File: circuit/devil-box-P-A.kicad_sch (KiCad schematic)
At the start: 17 parts, among them M1 Motor_Servo, SW1 SW_Push, T1 BSS83P, T2 BSS83P, T3 BSS83P, T4 BUZ11, T5 BSS83P

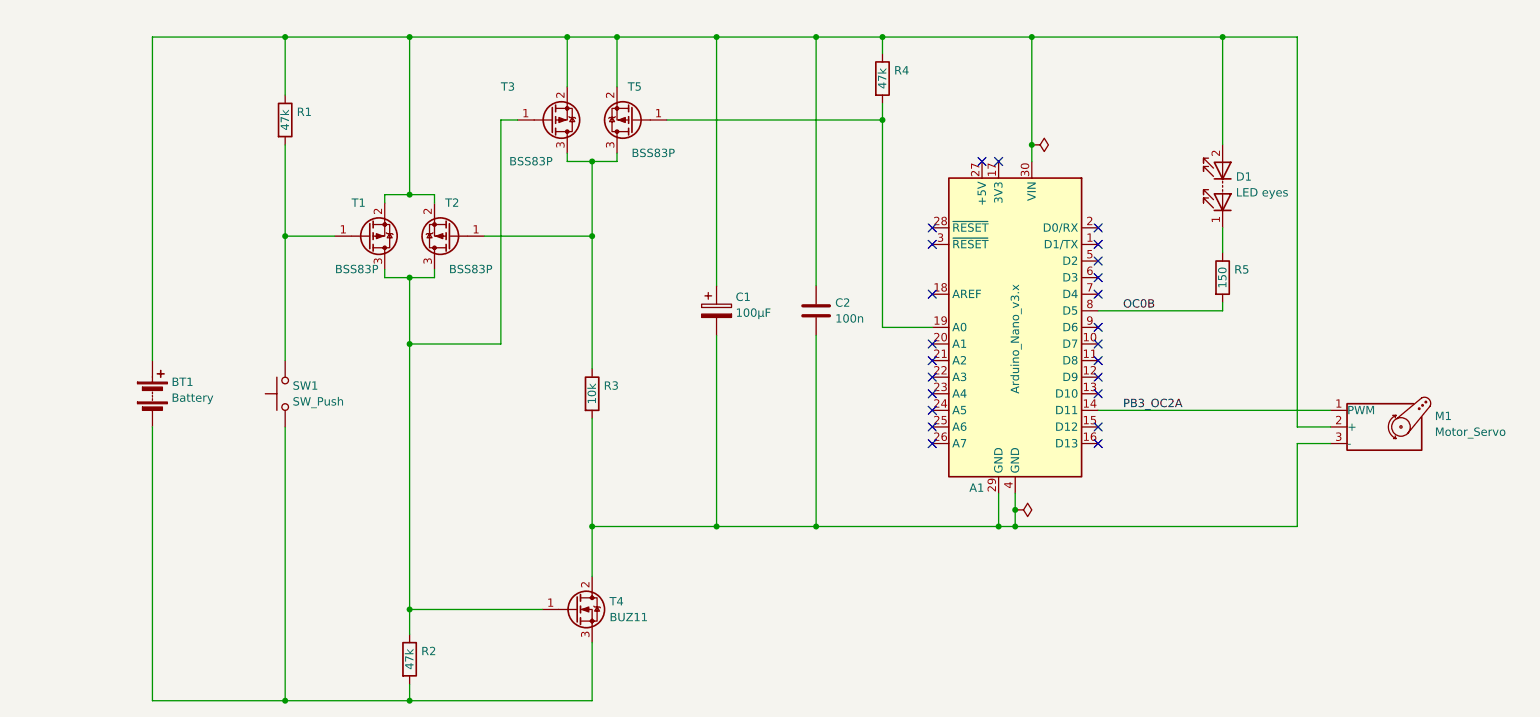
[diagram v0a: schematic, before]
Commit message: complementar option added
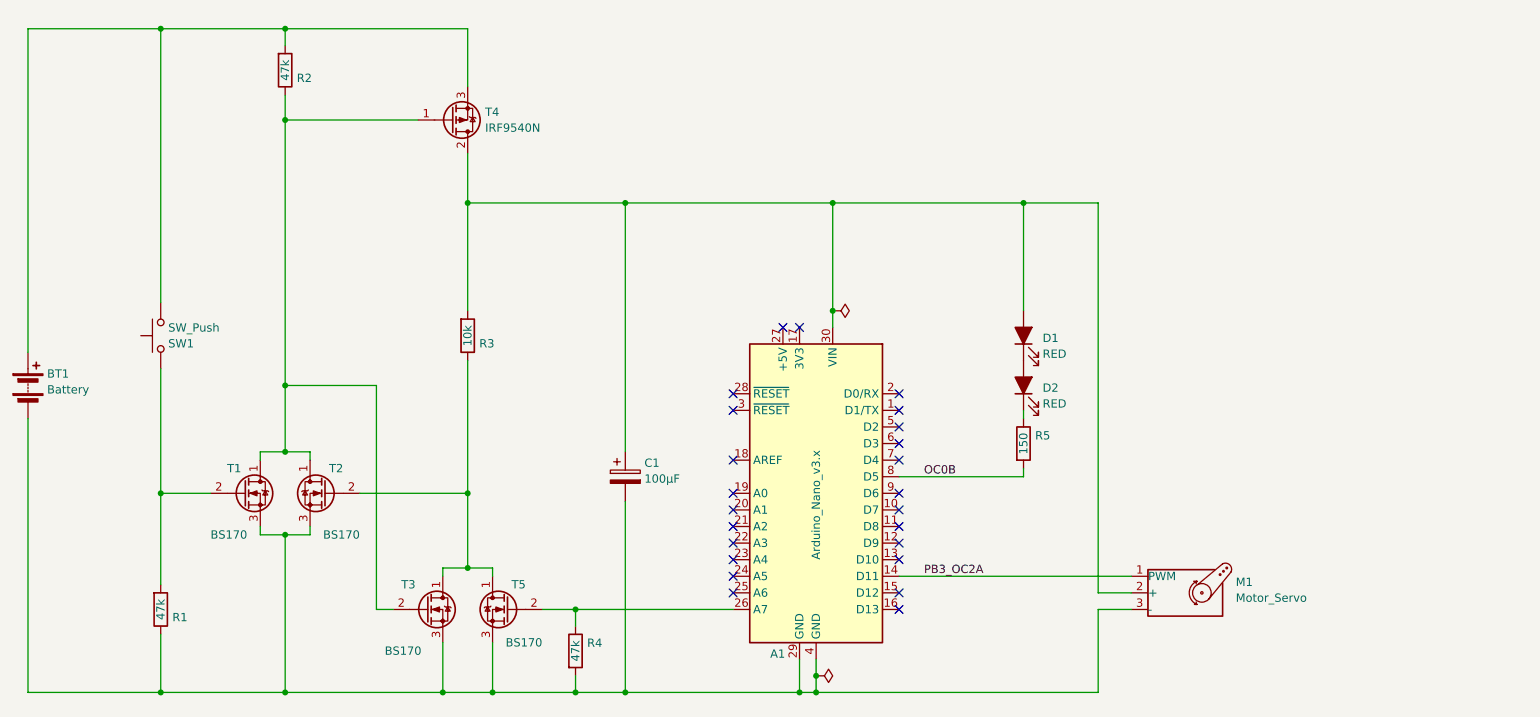
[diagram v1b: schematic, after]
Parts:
- removed C2: 100n, Misi:C_Polstarek_L12mm_W2mm_P5mm, symbol Device:C
- removed D1: LED eyes, Connector_PinHeader_2.54mm:PinHeader_1x02_P2.54mm_Vertical, symbol Device:LED_Series
- removed T1, T2, T3, T5: BSS83P, Package_TO_SOT_SMD:SOT-23, symbol Transistor_FET:BSS83P
- removed T4: BUZ11, Package_TO_SOT_THT:TO-220-3_Vertical, symbol Transistor_FET:BUZ11
- added D1, D2: RED, Connector_PinHeader_2.54mm:PinHeader_1x02_P2.54mm_Vertical, symbol Device:LED_Filled
- added T1, T2, T3, T5: BS170, Package_TO_SOT_THT:TO-92_Inline, symbol Transistor_FET:BS170
- added T4: IRF9540N, Package_TO_SOT_THT:TO-220-3_Vertical, symbol Transistor_FET:IRF9540N
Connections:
- net at R2.1: now also T1.1 (D), T2.1 (D), T3.2 (G), T4.1 (G)
- net at A1.30 (VIN), C1.1, M1.2 (+): now also R3.2, D1.2 (A), T4.2 (D); no longer BT1.1 (+), R1.1, R4.1
- net at R3.1: now also T2.2 (G), T3.1 (D), T5.1 (D)
- net at R2.2, SW1.1: now also BT1.1 (+), T4.3 (S); no longer BT1.2 (-)
- net at R1.2, SW1.2: now also T1.2 (G)
- net at A1.29 (GND), A1.4 (GND), C1.2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: now also BT1.2 (-), R1.1, R4.2, T1.3 (S), T2.3 (S), T3.3 (S), T5.3 (S); no longer R3.2
- net at R5.1: now also D2.1 (K)
- net at A1.19 (A0): no longer R4.2
- net at A1.26 (A7): now also R4.1, T5.2 (G)
- new net: D1.1 (K), D2.2 (A)
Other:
- title: Devil box -> (none)
- moved on the sheet: A1, BT1, C1, M1, R1, R2, R3, R4, R5, SW1

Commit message: main MOSFET changed
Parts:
- T4: value IRF9540N -> IRF9Z34N
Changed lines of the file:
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@@
 		(fields_autoplaced yes)
 		(property "Reference" "T4"
-			(at 115.697 53.3979 0)
+			(at 115.697 53.3978 0)
 			(effects
 				(font
@@
 			)
 		)
-		(property "Value" "IRF9540N"
+		(property "Value" "IRF9Z34N"
 			(at 115.697 55.8221 0)
 			(effects

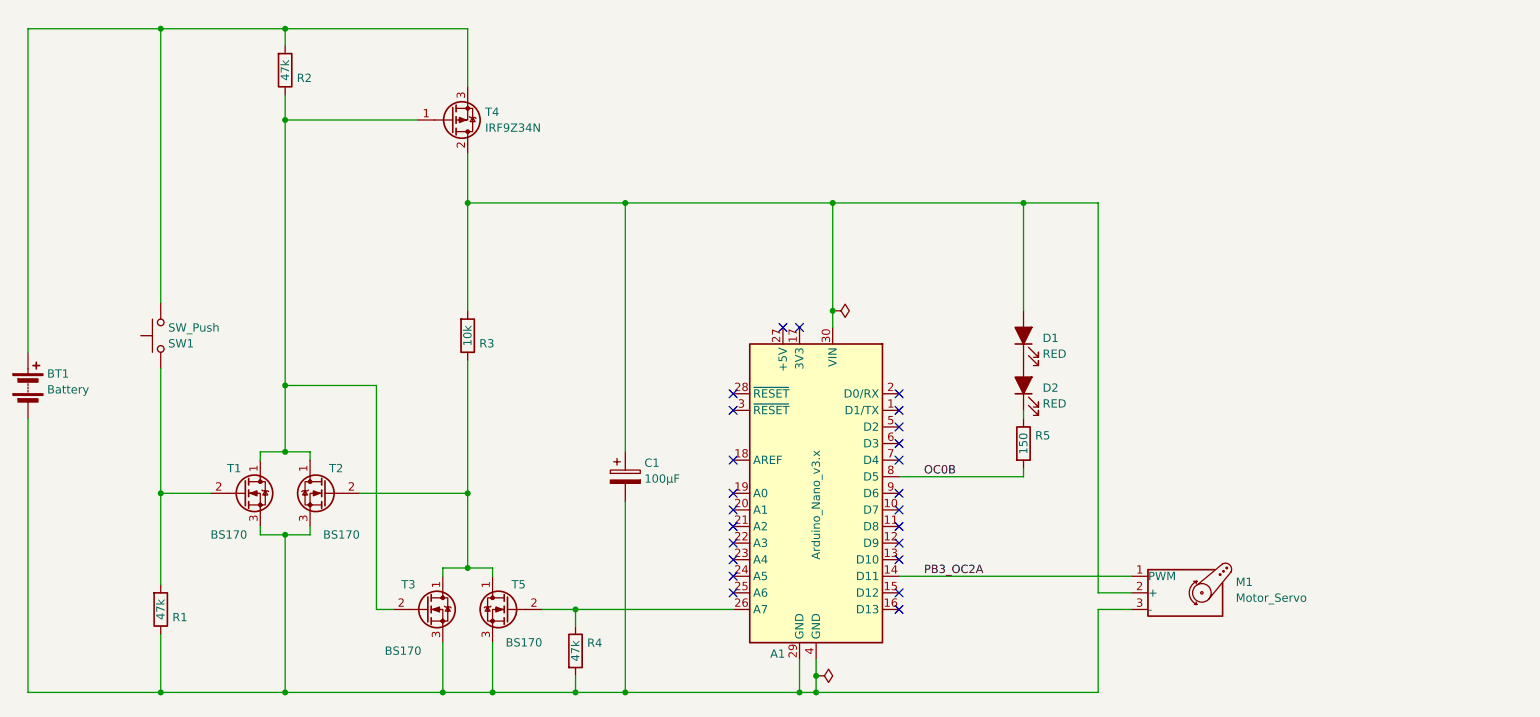
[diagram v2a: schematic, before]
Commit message: PCB created for P variant
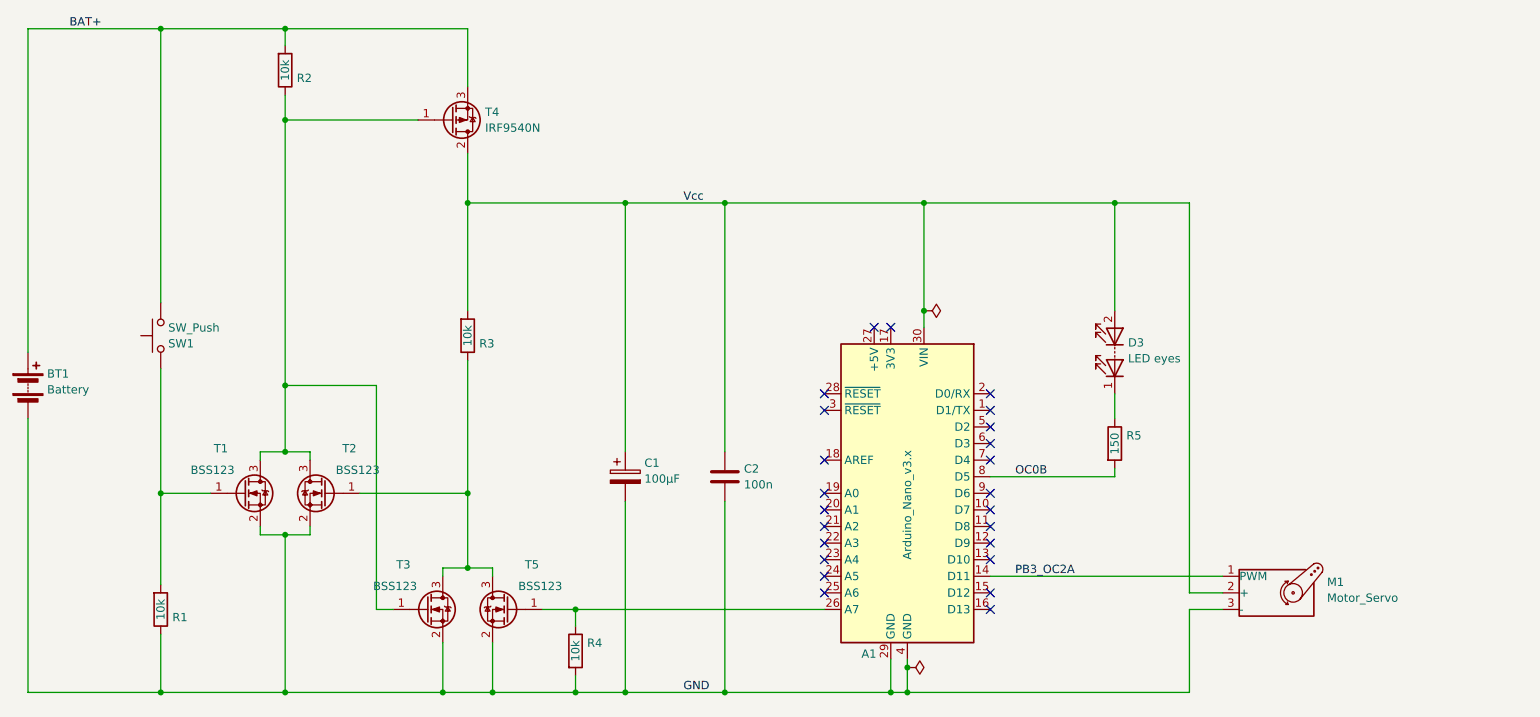
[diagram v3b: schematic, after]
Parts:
- removed D1, D2: RED, Connector_PinHeader_2.54mm:PinHeader_1x02_P2.54mm_Vertical, symbol Device:LED_Filled
- removed T1, T2, T3, T5: BS170, Package_TO_SOT_THT:TO-92_Inline, symbol Transistor_FET:BS170
- added C2: 100n, Capacitor_THT:C_Disc_D5.0mm_W2.5mm_P5.00mm, symbol Device:C
- added D3: LED eyes, Connector_PinHeader_2.54mm:PinHeader_1x02_P2.54mm_Vertical, symbol Device:LED_Series
- added T1, T2, T3, T5: BSS123, Package_TO_SOT_SMD:SOT-23, symbol Transistor_FET:BSS123
- A1: footprint Module:Arduino_Nano -> Module:Arduino_Nano_WithMountingHoles
- C1: footprint (none) -> Capacitor_THT:CP_Radial_D5.0mm_P2.50mm
- R1, R2, R4: value 47k -> 10k; footprint Resistor_THT:R_Axial_DIN0309_L9.0mm_D3.2mm_P12.70mm_Horizontal -> Resistor_SMD:R_0603_1608Metric
- R3: footprint Resistor_THT:R_Axial_DIN0309_L9.0mm_D3.2mm_P12.70mm_Horizontal -> Resistor_SMD:R_0603_1608Metric
- R5: footprint Resistor_THT:R_Axial_DIN0309_L9.0mm_D3.2mm_P12.70mm_Horizontal -> Resistor_SMD:R_0805_2012Metric
- SW1: footprint Connector_PinHeader_2.54mm:PinHeader_1x02_P2.54mm_Vertical -> Resistor_THT:R_Axial_DIN0617_L17.0mm_D6.0mm_P20.32mm_Horizontal
- T4: value IRF9Z34N -> IRF9540N; footprint Package_TO_SOT_THT:TO-220-3_Vertical -> Package_TO_SOT_THT:TO-220-3_Horizontal_TabDown
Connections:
- net BAT+: now reaches BT1.1 (+), R2.2, SW1.1, T4.3 (S)
- net at R1.2, SW1.2: now also T1.1 (G)
- net at R5.1: now also D3.1 (K)
- net Vcc: now reaches A1.30 (VIN), C1.1, M1.2 (+), R3.2, T4.2 (D)
- net Vcc: now also C2.1, D3.2 (A)
- net GND: now reaches A1.29 (GND), A1.4 (GND), BT1.2 (-), C1.2, M1.3 (-), R1.1, R4.2
- net GND: now also C2.2, T1.2 (S), T2.2 (S), T3.2 (S), T5.2 (S)
- net at R2.1, T4.1 (G): now also T1.3 (D), T2.3 (D), T3.1 (G)
- net at R3.1: now also T2.1 (G), T3.3 (D), T5.3 (D)
- net at A1.26 (A7), R4.1: now also T5.1 (G)
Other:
- title: (none) -> Devil box
- moved on the sheet: A1, M1, R5
